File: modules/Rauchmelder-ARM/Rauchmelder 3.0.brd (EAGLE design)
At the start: 38 x 65 mm, 61 parts, among them IC2 LPC1115, IC3 BD9G101, Q1 BC856, Q3 BCP52, Q4 ASFL, T1 BC848

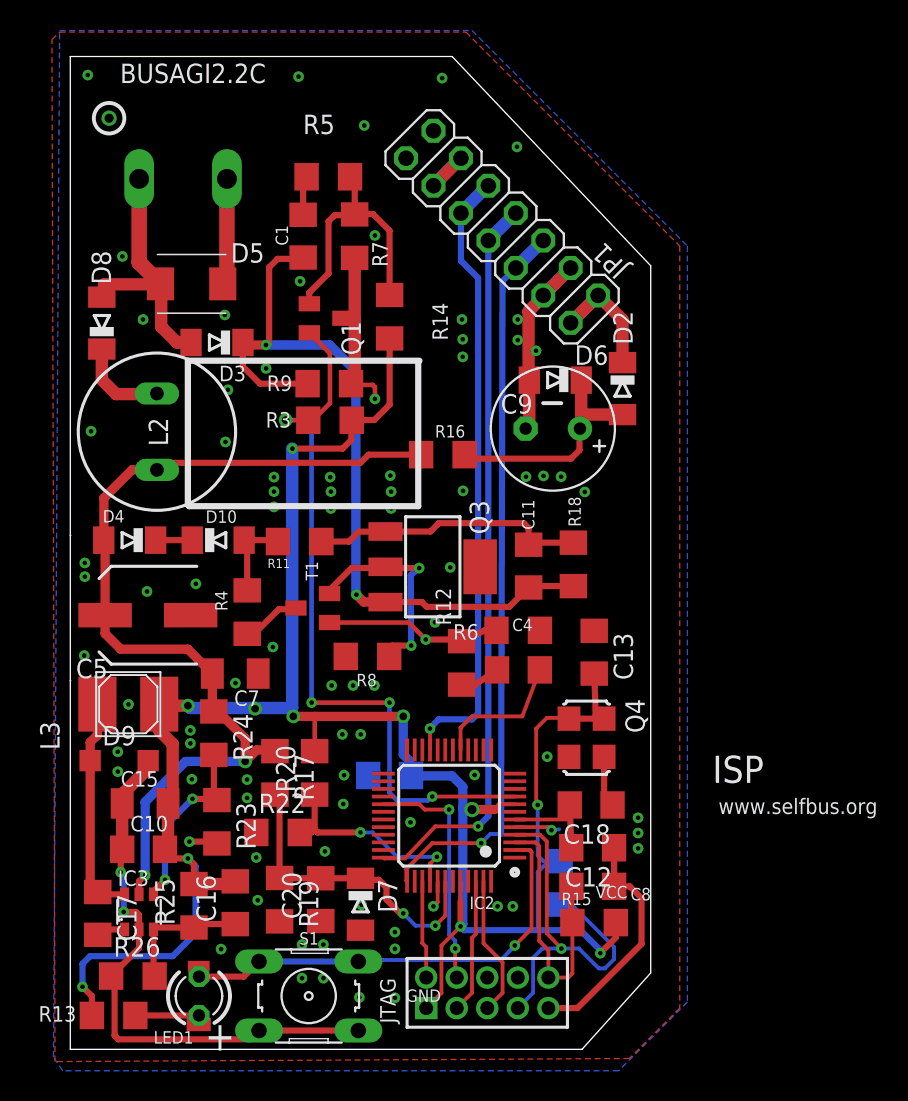
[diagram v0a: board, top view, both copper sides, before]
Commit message: Beschriftungen geändert
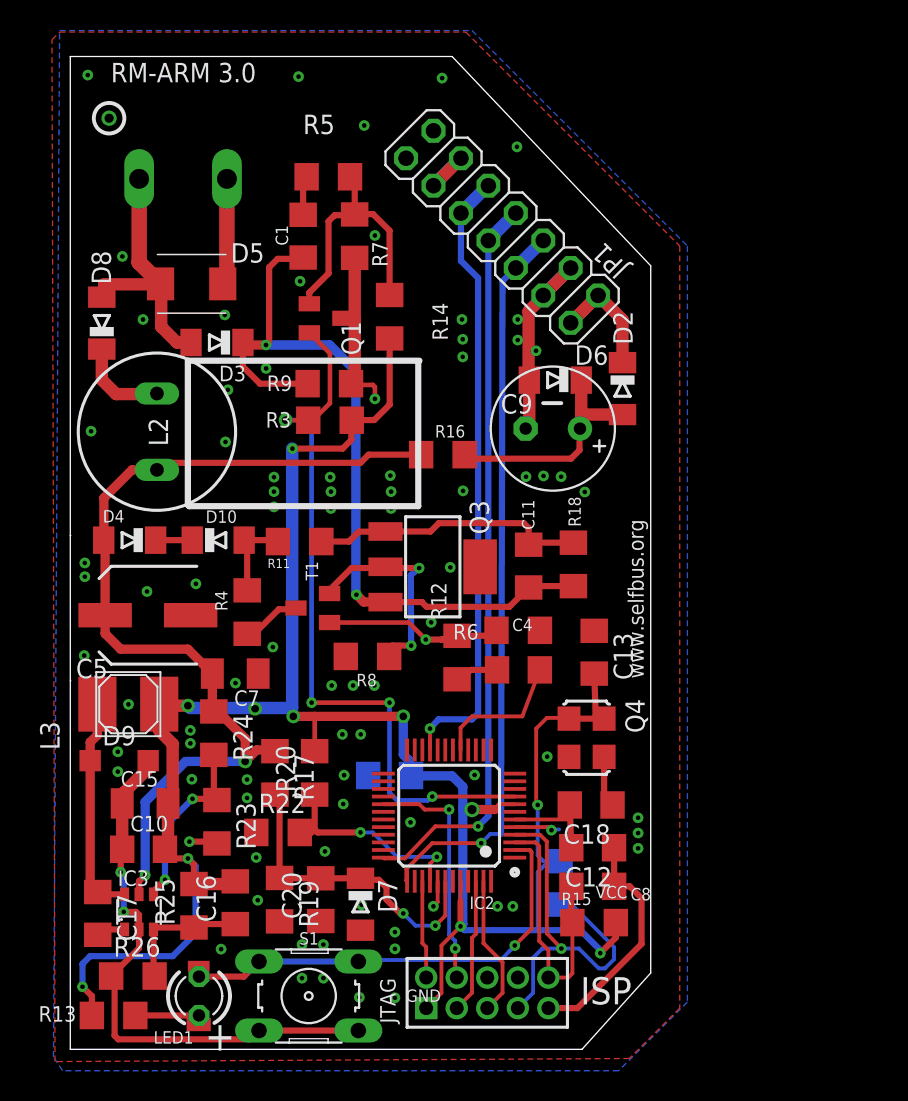
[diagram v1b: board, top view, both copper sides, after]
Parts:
- moved R12 0.46 mm to (25.3, 25.6)
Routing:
- net N$34: track 12.9 -> 11.5 mm
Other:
- board text added: "RM-ARM 3.0"
- board text removed: "BUSAGI2.2C"

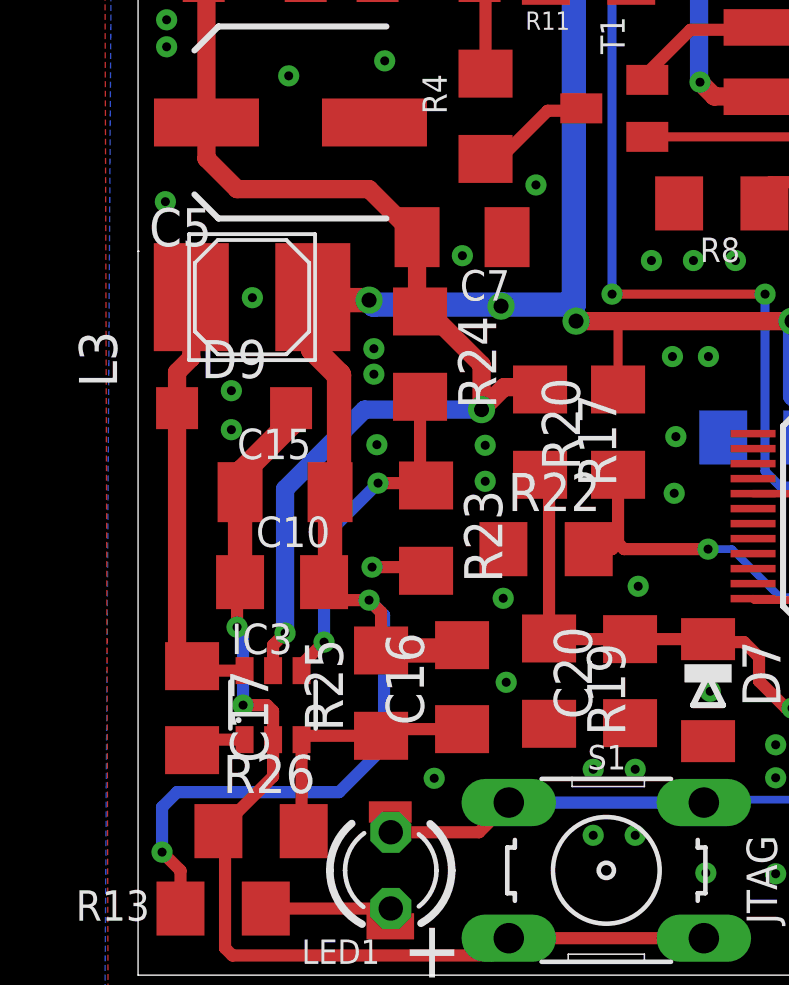
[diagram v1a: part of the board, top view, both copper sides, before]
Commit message: C7 verschoben
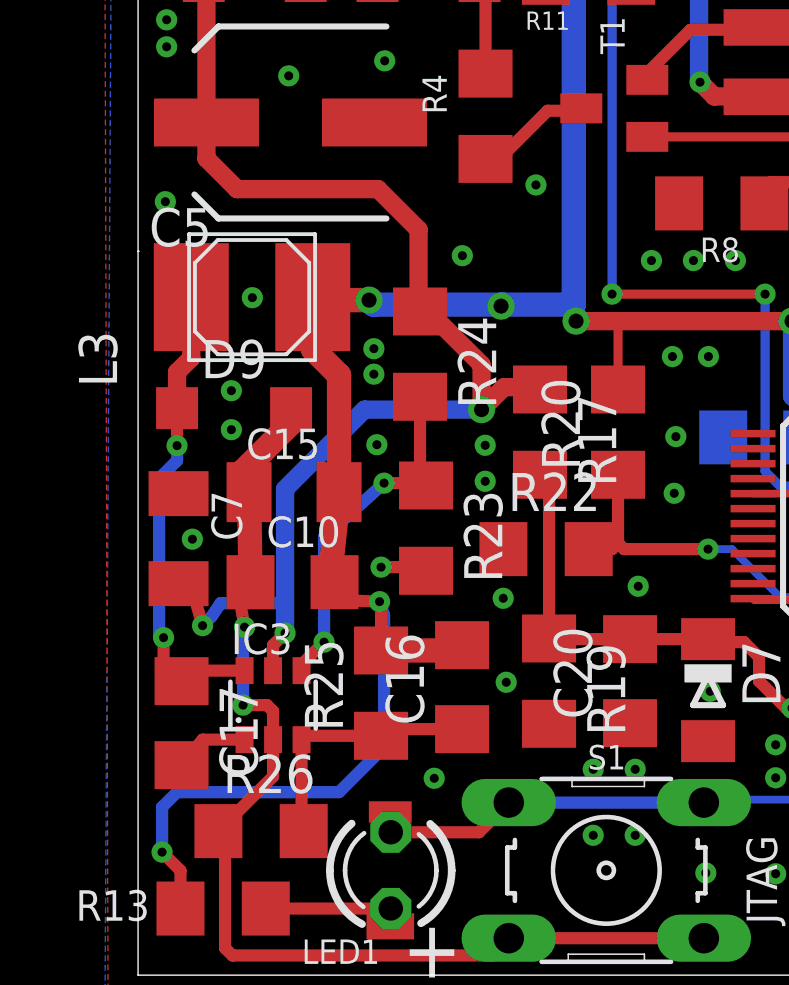
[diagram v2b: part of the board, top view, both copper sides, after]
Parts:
- moved C7 13.8 mm to (1.35, 14.6), turned to 270 degrees
- moved C17 0.61 mm to (1.45, 8.40)
- moved C10 0.35 mm to (5.15, 13.1)
- moved C15 0.30 mm to (5.20, 16.1)
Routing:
- net EIB_DC: track 62.3 -> 67.3 mm, vias 2 -> 3
- net LX: track 14.5 -> 15.8 mm, vias 0 -> 2
- net N$19: track 1.89 -> 2.50 mm
- net GND: track 89.4 -> 89.5 mm, vias 86 -> 87
